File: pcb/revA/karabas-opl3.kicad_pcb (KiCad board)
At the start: 2 copper layers, 98.2 x 64 mm, 82 parts, among them J1 Conn_02x05_Odd_Even, J2 Conn_02x30_Row_Letter_First, J3 PJ307, J4 Conn_01x04, J5 5V_PRG, SW1 SW_DIP_x05, U1 YMF262-M, U2 74AHCT1G125DB, U3 EPM3128ATC100, U4 UDA1334ATS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

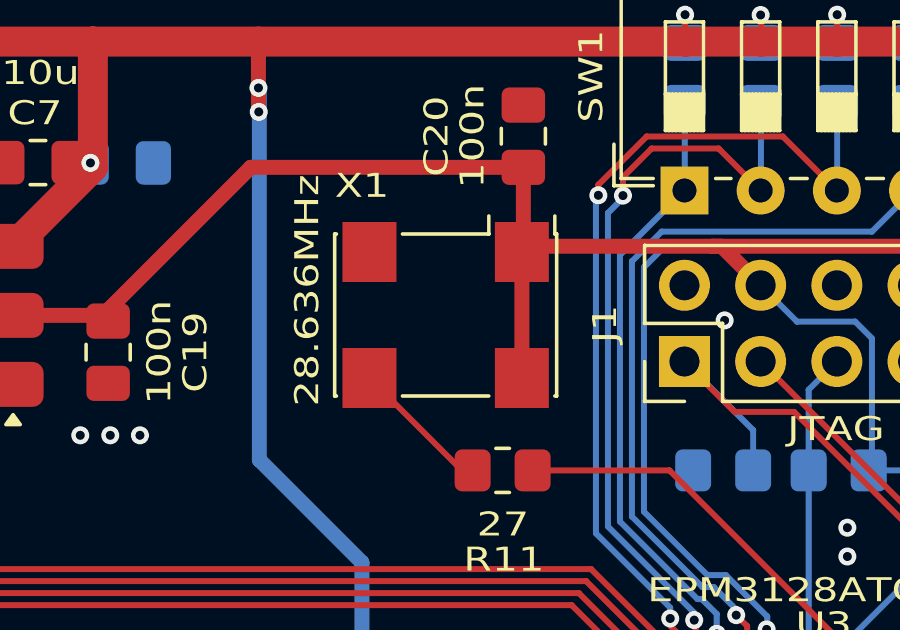
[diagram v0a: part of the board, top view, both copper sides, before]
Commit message: Added universal footprint for 3225+5070 osc
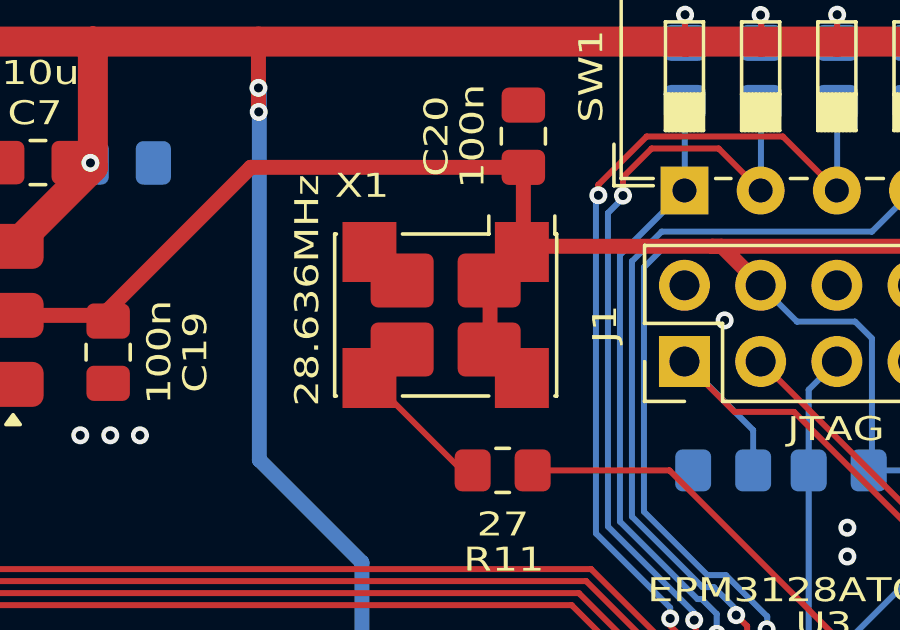
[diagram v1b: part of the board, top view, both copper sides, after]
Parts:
- X1: footprint my:Oscillator_SMD_7050_7.0x5.0mm -> footprints:Oscillator_SMD_7050_7.0x5.0mm_mixed_3225
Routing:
- net +3V3: track 173.3 -> 174.2 mm
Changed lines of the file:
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@@
 		)
 	)
-	(footprint "my:Oscillator_SMD_7050_7.0x5.0mm"
+	(footprint "footprints:Oscillator_SMD_7050_7.0x5.0mm_mixed_3225"
 		(layer "F.Cu")
 		(at 161.12 84.99 180)
@@
 			(pintype "input")
 		)
+		(pad "1" smd roundrect
+			(at -1.45 1.15 180)
+			(size 2.1 1.8)
+			(layers "F.Cu" "F.Mask" "F.Paste")
+			(roundrect_rratio 0.138889)
+			(net 3 "+3V3")
+			(pinfunction "EN")
+			(pintype "input")
+		)
+		(pad "2" smd roundrect
+			(at 1.45 1.15 180)
+			(size 2.1 1.8)
+			(layers "F.Cu" "F.Mask" "F.Paste")
+			(roundrect_rratio 0.138889)
+			(net 1 "GND")
+			(pinfunction "GND")
+			(pintype "power_in")
+		)
 		(pad "2" smd rect
 			(at 2.54 2.1 180)
@@
 			(pintype "power_in")
 		)
+		(pad "3" smd roundrect
+			(at 1.45 -1.15 180)
+			(size 2.1 1.8)
+			(layers "F.Cu" "F.Mask" "F.Paste")
+			(roundrect_rratio 0.138889)
+			(net 52 "Net-(X1-OUT)")
+			(pinfunction "OUT")
+			(pintype "output")
+		)
 		(pad "3" smd rect
 			(at 2.54 -2.1 180)
@@
 			(pintype "power_in")
 		)
+		(pad "4" smd roundrect
+			(at -1.45 -1.15 180)
+			(size 2.1 1.8)
+			(layers "F.Cu" "F.Mask" "F.Paste")
+			(roundrect_rratio 0.138889)
+			(net 3 "+3V3")
+			(pinfunction "V+")
+			(pintype "power_in")
+		)
 		(embedded_fonts no)
 		(model "${KICAD6_3DMODEL_DIR}/Oscillator.3dshapes/Oscillator_SMD_Abracon_ASV-4Pin_7.0x5.1mm.wrl"
@@
 	)
 	(segment
-		(start 163.66 82.89)
-		(end 163.66 87.09)
-		(width 0.5)
-		(layer "F.Cu")
-		(net 3)
-	)
-	(segment
 		(start 171.62 84)
 		(end 170.319 82.699)
@@
 	)
 	(segment
+		(start 162.6 83.95)
+		(end 162.6 86.03)
+		(width 0.5)
+		(layer "F.Cu")
+		(net 3)
+	)
+	(segment
 		(start 181.81 83.98)
 		(end 181.85 84.02)
@@
 	)
 	(segment
+		(start 163.66 82.89)
+		(end 162.6 83.95)
+		(width 0.5)
+		(layer "F.Cu")
+		(net 3)
+	)
+	(segment
 		(start 140.42 85.38)
 		(end 140.3425 85.4575)
 		(width 0.5)
 		(layer "F.Cu")
+		(net 3)
+	)
+	(segment
+		(start 162.6 86.03)
+		(end 163.66 87.09)
+		(width 0.5)
+		(layer "F.Cu")

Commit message: Updated 5V lane - removed loop
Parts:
- added TP1: +5V, TestPoint:TestPoint_Keystone_5015_Micro_Mini, B.Cu at (113.8, 124.1)
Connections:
- J2 pad a3: +5V -> Net-(J2-Pin_a3)
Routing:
- net +5V: track 275.7 -> 209.1 mm, vias 17 -> 14
- net Net-(J2-Pin_a3): track 0.00 -> 6.96 mm
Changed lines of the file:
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@@
 	(net 140 "LED2")
 	(net 141 "Net-(D2-A)")
+	(net 142 "Net-(J2-Pin_a3)")
 	(footprint "Capacitor_SMD:C_0805_2012Metric_Pad1.18x1.45mm_HandSolder"
 		(layer "F.Cu")
@@
 			(chamfer_ratio 0.2)
 			(chamfer top_left top_right bottom_left bottom_right)
-			(net 2 "+5V")
+			(net 142 "Net-(J2-Pin_a3)")
 			(pinfunction "Pin_a3")
 			(pintype "passive")
@@
 		)
 	)
+	(footprint "TestPoint:TestPoint_Keystone_5015_Micro_Mini"
+		(layer "B.Cu")
+		(at 113.8 124.1)
+		(descr "Keystone SMT Micro Mini Test Point 5015, http://www.keyelco.com/product-pdf.cfm?p=1353")
+		(tags "Test Point")
+		(property "Reference" "TP1"
+			(at 0 -3.5 180)
+			(layer "B.SilkS")
+			(effects
+				(font
+					(size 0.8 1)
+					(thickness 0.15)
+				)
+				(justify mirror)
+			)
+		)
+		(property "Value" "+5V"
+			(at 0 -2.25 180)
+			(layer "B.SilkS")
+			(effects
+				(font
+					(size 0.8 1)
+					(thickness 0.15)
+				)
+				(justify mirror)
+			)
+		)
+		(property "Datasheet" "~"
+			(at 0 0 180)
+			(unlocked yes)
+			(layer "B.Fab")
+			(hide yes)
+			(effects
+				(font
+					(size 1.27 1.27)
+					(thickness 0.15)
+				)
+				(justify mirror)
+			)
+		)
+		(property "Description" "test point"
+			(at 0 0 180)
+			(unlocked yes)
+			(layer "B.Fab")
+			(hide yes)
+			(effects
+				(font
+					(size 1.27 1.27)
+					(thickness 0.15)
+				)
+				(justify mirror)
+			)
+		)
+		(property ki_fp_filters "Pin* Test*")
+		(sheetname "/")
+		(sheetfile "karabas-opl3.kicad_sch")
+		(attr smd)
+		(fp_rect
+			(start -1.9 1.1)
+			(end 1.9 -1.1)
+			(stroke
+				(width 0.12)
+				(type default)
+			)
+			(fill no)
+			(layer "B.SilkS")
+		)
+		(fp_line
+			(start -2.15 -1.35)
+			(end -2.15 1.35)
+			(stroke
+				(width 0.05)
+				(type solid)
+			)
+			(layer "B.CrtYd")
+		)
+		(fp_line
+			(start -2.15 1.35)
+			(end 2.15 1.35)
+			(stroke
+				(width 0.05)
+				(type solid)
+			)
+			(layer "B.CrtYd")
+		)
+		(fp_line
+			(start 2.15 -1.35)
+			(end -2.15 -1.35)
+			(stroke
+				(width 0.05)
+				(type solid)
+			)
+			(layer "B.CrtYd")
+		)
+		(fp_line
+			(start 2.15 1.35)
+			(end 2.15 -1.35)
+			(stroke
+				(width 0.05)
+				(type solid)
+			)
+			(layer "B.CrtYd")
+		)
+		(fp_rect
+			(start -1.35 0.5)
+			(end 1.35 -0.5)
+			(stroke
+				(width 0.1)
+				(type default)
+			)
+			(fill no)
+			(layer "B.Fab")
+		)
+		(fp_text user "${REFERENCE}"
+			(at 0 0 180)
+			(layer "B.Fab")
+			(effects
+				(font
+					(size 0.6 0.6)
+					(thickness 0.09)
+				)
+				(justify mirror)
+			)
+		)
+		(pad "1" smd roundrect
+			(at 0 0)
+			(size 3.4 1.8)
+			(layers "B.Cu" "B.Mask" "B.Paste")
+			(roundrect_rratio 0.1388888889)
+			(net 142 "Net-(J2-Pin_a3)")
+			(pinfunction "1")
+			(pintype "passive")
+		)
+		(embedded_fonts no)
+		(model "${KICAD9_3DMODEL_DIR}/TestPoint.3dshapes/TestPoint_Keystone_5015_Micro_Mini.step"
+			(offset
+				(xyz 0 0 0)
+			)
+			(scale
+				(xyz 1 1 1)
+			)
+			(rotate
+				(xyz 0 0 0)
+			)
+		)
+	)
 	(footprint "Resistor_SMD:R_0805_2012Metric_Pad1.20x1.40mm_HandSolder"
 		(layer "B.Cu")
@@
 	)
 	(segment
-		(start 136.14 80.76)
-		(end 136.14 81.65)
-		(width 1)
-		(layer "F.Cu")
-		(net 2)
-	)
-	(segment
 		(start 171.64 75.8765)
 		(end 169.11 75.8765)
@@
 	)
 	(segment
-		(start 136.14 75.9265)
-		(end 136.09 75.8765)
-		(width 1)
-		(layer "F.Cu")
-		(net 2)
-	)
-	(segment
 		(start 149.36 75.8765)
 		(end 136.09 75.8765)
@@
 	)
 	(segment
-		(start 136.14 79.89)
-		(end 136.14 80.76)
-		(width 1)
-		(layer "F.Cu")
-		(net 2)
-	)
-	(segment
 		(start 154.88 75.8765)
 		(end 149.36 75.8765)
@@
 	)
 	(segment
-		(start 136.14 79.89)
-		(end 136.14 75.9265)
-		(width 1)
-		(layer "F.Cu")
-		(net 2)
-	)
-	(segment
 		(start 180.4 117.42698)
 		(end 179.55 117.42698)
@@
 	)
 	(via
-		(at 136.14 81.65)
-		(size 0.6)
-		(drill 0.3)
-		(layers "F.Cu" "B.Cu")
-		(net 2)
-	)
-	(via
 		(at 179.26 74.98)
 		(size 0.6)
@@
 	)
 	(via
-		(at 136.14 79.89)
-		(size 0.6)
-		(drill 0.3)
-		(layers "F.Cu" "B.Cu")
-		(net 2)
-	)
-	(via
 		(at 154.89 78.22)
 		(size 0.6)
@@
 	)
 	(via
-		(at 136.14 80.76)
-		(size 0.6)
-		(drill 0.3)
-		(layers "F.Cu" "B.Cu")
-		(net 2)
-	)
-	(via
 		(at 178.4 127)
 		(size 0.8)
@@
 	)
 	(segment
-		(start 136.12 79.91)
-		(end 136.14 79.89)
-		(width 1)
-		(layer "B.Cu")
-		(net 2)
-	)
-	(segment
 		(start 176.71 75.92)
 		(end 176.71 75)
@@
 	)
 	(segment
-		(start 113.775 128.155)
-		(end 136.12 105.81)
-		(width 1)
-		(layer "B.Cu")
-		(net 2)
-	)
-	(segment
-		(start 113.775 131.49)
-		(end 113.775 128.155)
-		(width 1)
-		(layer "B.Cu")
-		(net 2)
-	)
-	(segment
 		(start 169.09 74.99)
 		(end 169.1 74.98)
@@
 	)
 	(segment
-		(start 136.12 105.81)
-		(end 136.12 79.91)
-		(width 1)
-		(layer "B.Cu")
-		(net 2)
-	)
-	(segment
 		(start 171.63 75.92)
 		(end 171.63 75)
@@
 		(net 141)
 	)
+	(segment
+		(start 113.775 131.49)
+		(end 113.7 131.415)
+		(width 1)
+		(layer "B.Cu")
+		(net 142)
+	)
+	(segment
+		(start 113.8 128.13)
+		(end 113.8 124.6)
+		(width 1)
+		(layer "B.Cu")
+		(net 142)
+	)
+	(segment
+		(start 113.7 131.415)
+		(end 113.7 128.23)
+		(width 1)
+		(layer "B.Cu")
+		(net 142)
+	)
+	(segment
+		(start 113.775 128.155)
+		(end 113.8 128.13)
+		(width 1)
+		(layer "B.Cu")
+		(net 142)
+	)
+	(segment
+		(start 113.7 128.23)
+		(end 113.775 128.155)
+		(width 1)
+		(layer "B.Cu")
+		(net 142)
+	)
 	(zone

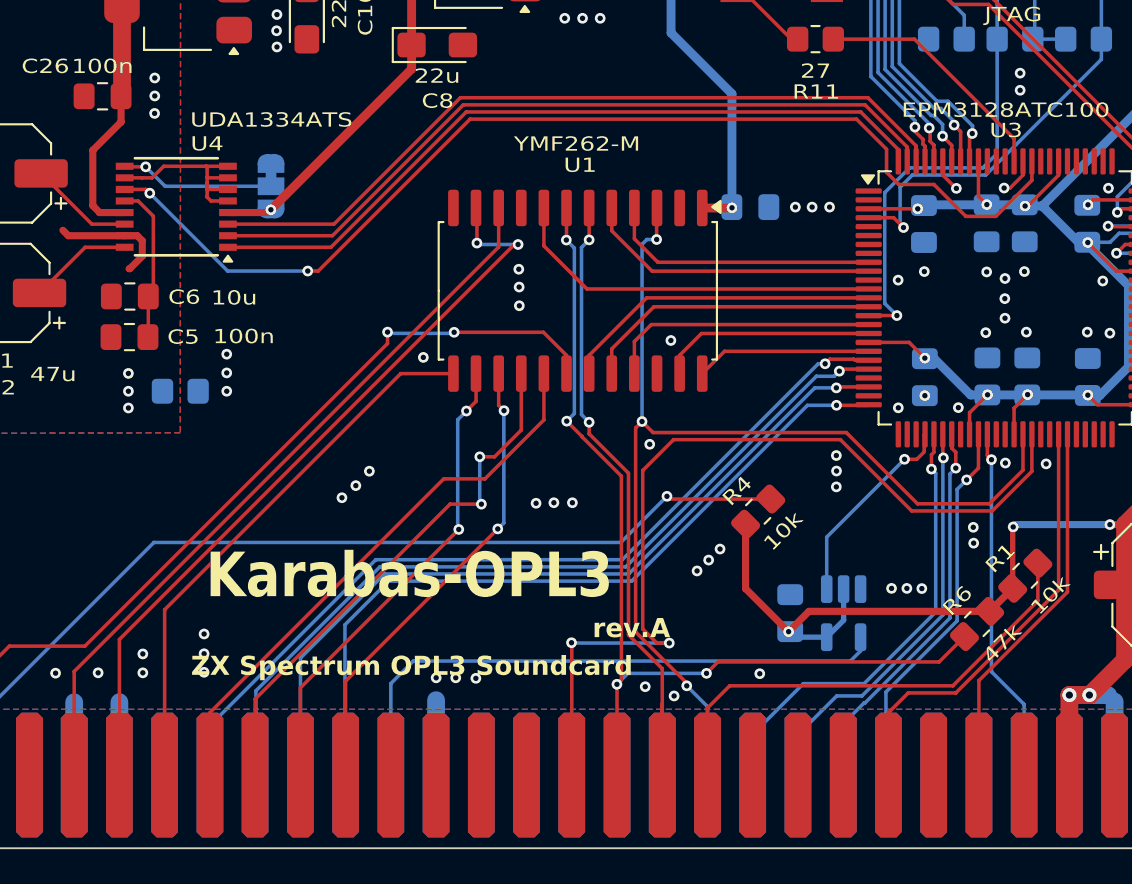
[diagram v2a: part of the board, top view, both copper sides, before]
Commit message: Small footprint fixes
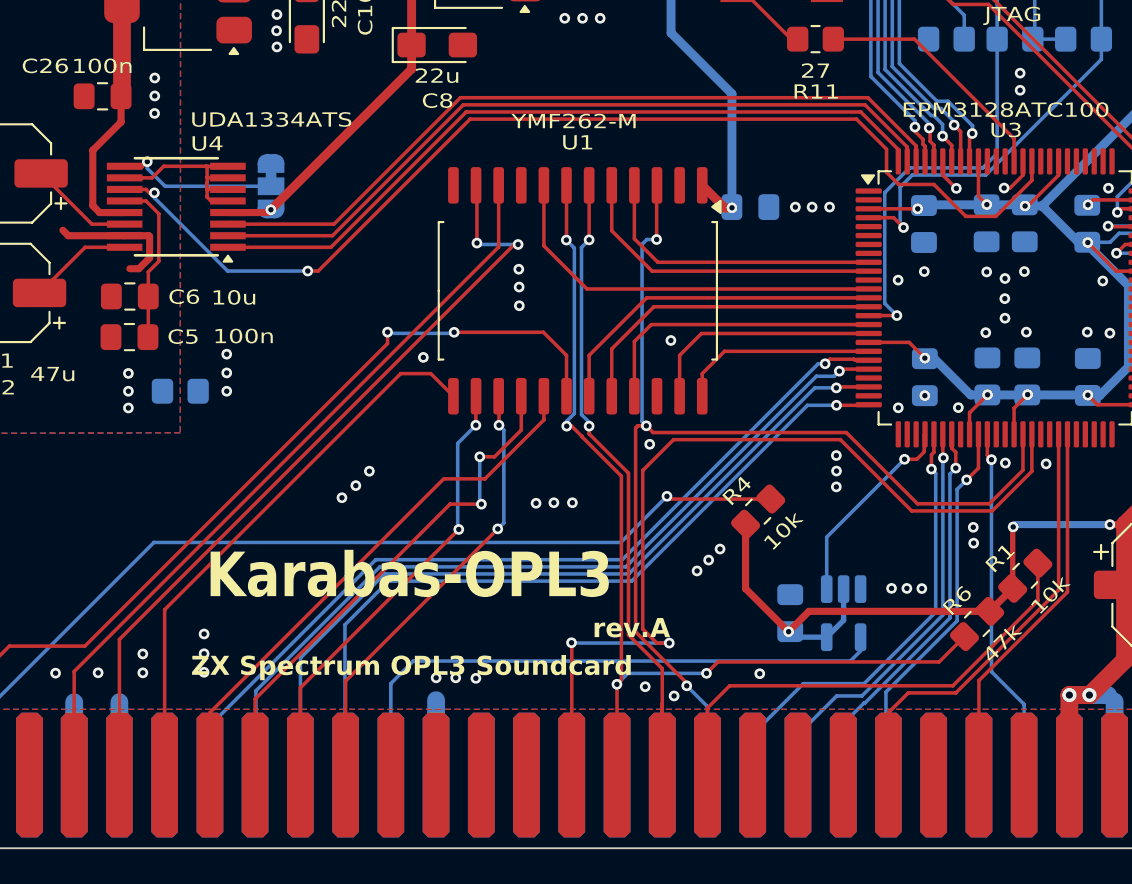
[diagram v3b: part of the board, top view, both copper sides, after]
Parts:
- U1: footprint Package_SO:SOIC-24W_7.5x15.4mm_P1.27mm -> footprints:ymf-262-m
- U4: footprint Package_SO:SSOP-16_4.4x5.2mm_P0.65mm -> footprints:SSOP-16_4.4x5.2mm_P0.65mm-extended
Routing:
- net D3: track 29.3 -> 27.7 mm
- net ~{RD}: track 56.8 -> 58.3 mm
- net ~{RST}: track 62.7 -> 64.1 mm
- net D4: track 29.0 -> 27.7 mm
- net ~{WR}: track 38.0 -> 39.2 mm
- net ~{YM_CS}: track 21.4 -> 22.6 mm
- net YM_A1: track 16.6 -> 17.9 mm
- net YM_A0: track 15.4 -> 16.7 mm
- net D0: track 44.3 -> 45.6 mm
- net YM_SMP2: track 18.1 -> 19.3 mm
- net YM_SMP1: track 16.8 -> 18.1 mm
- net YM_DCLK: track 12.2 -> 13.4 mm
- net D7: track 52.1 -> 53.4 mm
- net D6: track 34.3 -> 33.0 mm
- net D1: track 46.1 -> 47.4 mm
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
